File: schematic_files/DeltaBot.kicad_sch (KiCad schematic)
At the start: 16 parts, among them J1 USB C PD Modulle, J2 LIDAR, J3 MOTOR_L, J4 MOTOR_R, SW1 SW_SPDT, U1 Radxa_ROCK5B, U2 Buck Converter

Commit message: Updated PCB layout
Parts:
- removed D1, D2: D, deltabot:D_DO-41_SOD81_P10.16mm_Horizontal, symbol Device:D
- removed J2: LIDAR, deltabot:PinHeader_1x07_P2.54mm_Vertical, symbol Connector_Generic:Conn_01x07
- added J2: Conn_01x05, Connector_PinHeader_2.54mm:PinHeader_1x05_P2.54mm_Vertical, symbol Connector_Generic:Conn_01x05
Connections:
- net +5V: now also J2.2 (Pin_2)
- net GND: now also J2.5 (Pin_5)
- net LIDAR_RX: now also J2.4 (Pin_4)
- net LIDAR_TX: now also J2.3 (Pin_3)

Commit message: Small changes
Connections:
- net +5V: now also J2.1 (Pin_1); no longer J2.2 (Pin_2)
- net GND: now also J2.4 (Pin_4); no longer J2.5 (Pin_5)
- net LIDAR_RX: now also J2.3 (Pin_3); no longer J2.4 (Pin_4)
- net LIDAR_TX: now also J2.2 (Pin_2); no longer J2.3 (Pin_3)
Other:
- moved on the sheet: C3, J2
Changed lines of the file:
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@@
 	)
 	(junction
-		(at 34.29 119.38)
+		(at 24.13 104.14)
 		(diameter 0)
 		(color 0 0 0 0)
@@
 	)
 	(junction
-		(at 24.13 110.49)
+		(at 34.29 113.03)
 		(diameter 0)
 		(color 0 0 0 0)
@@
 	(wire
 		(pts
-			(xy 22.86 68.58) (xy 22.86 69.85)
+			(xy 34.29 113.03) (xy 34.29 114.3)
 		)
 		(stroke
@@
 	(wire
 		(pts
-			(xy 24.13 119.38) (xy 34.29 119.38)
+			(xy 22.86 68.58) (xy 22.86 69.85)
 		)
 		(stroke
@@
 	(wire
 		(pts
-			(xy 101.6 76.2) (xy 106.68 76.2)
+			(xy 24.13 113.03) (xy 34.29 113.03)
 		)
 		(stroke
@@
 	(wire
 		(pts
-			(xy 24.13 110.49) (xy 44.45 110.49)
+			(xy 101.6 76.2) (xy 106.68 76.2)
 		)
 		(stroke
@@
 	(wire
 		(pts
+			(xy 39.37 107.95) (xy 43.18 107.95)
+		)
+		(stroke
+			(width 0)
+			(type default)
+		)
+	)
+	(wire
+		(pts
 			(xy 66.04 64.77) (xy 76.2 64.77)
 		)
@@
 	(wire
 		(pts
-			(xy 34.29 119.38) (xy 40.64 119.38)
+			(xy 66.04 72.39) (xy 77.47 72.39)
 		)
 		(stroke
@@
 	(wire
 		(pts
-			(xy 66.04 72.39) (xy 77.47 72.39)
+			(xy 43.18 113.03) (xy 34.29 113.03)
 		)
 		(stroke
@@
 	(wire
 		(pts
-			(xy 68.58 97.79) (xy 68.58 102.87)
+			(xy 24.13 104.14) (xy 43.18 104.14)
 		)
 		(stroke
@@
 	(wire
 		(pts
-			(xy 104.14 83.82) (xy 106.68 83.82)
+			(xy 68.58 97.79) (xy 68.58 102.87)
 		)
 		(stroke
@@
 	(wire
 		(pts
-			(xy 66.04 102.87) (xy 68.58 102.87)
+			(xy 104.14 83.82) (xy 106.68 83.82)
 		)
 		(stroke
@@
 	(wire
 		(pts
-			(xy 40.64 119.38) (xy 40.64 118.11)
+			(xy 66.04 102.87) (xy 68.58 102.87)
 		)
 		(stroke
@@
 	(wire
 		(pts
-			(xy 24.13 111.76) (xy 24.13 110.49)
+			(xy 24.13 105.41) (xy 24.13 104.14)
 		)
 		(stroke
@@
 	(wire
 		(pts
-			(xy 34.29 120.65) (xy 34.29 119.38)
-		)
-		(stroke
-			(width 0)
-			(type default)
-		)
-	)
-	(wire
-		(pts
 			(xy 46.99 72.39) (xy 46.99 68.58)
 		)
@@
 	(wire
 		(pts
-			(xy 39.37 113.03) (xy 44.45 113.03)
-		)
-		(stroke
-			(width 0)
-			(type default)
-		)
-	)
-	(wire
-		(pts
 			(xy 22.86 64.77) (xy 25.4 64.77)
 		)
@@
 	(wire
 		(pts
+			(xy 39.37 110.49) (xy 43.18 110.49)
+		)
+		(stroke
+			(width 0)
+			(type default)
+		)
+	)
+	(wire
+		(pts
 			(xy 71.12 34.29) (xy 73.66 34.29)
 		)
@@
 	(wire
 		(pts
-			(xy 39.37 115.57) (xy 44.45 115.57)
-		)
-		(stroke
-			(width 0)
-			(type default)
-		)
-	)
-	(wire
-		(pts
 			(xy 168.91 26.67) (xy 176.53 26.67)
 		)
@@
 	(wire
 		(pts
-			(xy 40.64 118.11) (xy 44.45 118.11)
+			(xy 168.91 35.56) (xy 167.64 35.56)
 		)
 		(stroke
@@
 	(wire
 		(pts
-			(xy 168.91 35.56) (xy 167.64 35.56)
+			(xy 71.12 31.75) (xy 71.12 34.29)
 		)
 		(stroke
@@
 	(wire
 		(pts
-			(xy 71.12 31.75) (xy 71.12 34.29)
+			(xy 43.18 105.41) (xy 43.18 104.14)
 		)
 		(stroke
@@
 	(wire
 		(pts
-			(xy 21.59 110.49) (xy 24.13 110.49)
+			(xy 21.59 104.14) (xy 24.13 104.14)
 		)
 		(stroke
@@
 	(global_label "LIDAR_TX"
 		(shape input)
-		(at 39.37 113.03 180)
+		(at 39.37 107.95 180)
 		(effects
 			(font
@@
 		)
 		(property "Intersheetrefs" "${INTERSHEET_REFS}"
-			(at 39.37 113.03 0)
+			(at 39.37 107.95 0)
 			(effects
 				(font
@@
 	(global_label "LIDAR_RX"
 		(shape input)
-		(at 39.37 115.57 180)
+		(at 39.37 110.49 180)
 		(effects
 			(font
@@
 		)
 		(property "Intersheetrefs" "${INTERSHEET_REFS}"
-			(at 39.37 115.57 0)
+			(at 39.37 110.49 0)
 			(effects
 				(font
@@
 	(symbol
 		(lib_id "power:GND")
-		(at 34.29 120.65 0)
+		(at 34.29 114.3 0)
 		(unit 1)
 		(exclude_from_sim no)
@@
 		(dnp no)
 		(property "Reference" "#PWR09"
-			(at 34.29 127 0)
+			(at 34.29 120.65 0)
 			(effects
 				(font
@@
 		)
 		(property "Value" "GND"
-			(at 34.417 125.0442 0)
+			(at 34.417 118.6942 0)
 			(effects
 				(font
@@
 		)
 		(property "Footprint" ""
-			(at 34.29 120.65 0)
+			(at 34.29 114.3 0)
 			(effects
 				(font
@@
 		)
 		(property "Datasheet" ""
-			(at 34.29 120.65 0)
+			(at 34.29 114.3 0)
 			(effects
 				(font
@@
 		)
 		(property "Description" ""
-			(at 34.29 120.65 0)
+			(at 34.29 114.3 0)
 			(effects
 				(font
@@
 	(symbol
 		(lib_id "power:+5V")
-		(at 21.59 110.49 90)
+		(at 21.59 104.14 90)
 		(unit 1)
 		(exclude_from_sim no)
@@
 		(dnp no)
 		(property "Reference" "#PWR08"
-			(at 25.4 110.49 0)
+			(at 25.4 104.14 0)
 			(effects
 				(font
@@
 		)
 		(property "Value" "+5V"
-			(at 18.3388 110.109 90)
+			(at 18.3388 103.759 90)
 			(effects
 				(font
@@
 		)
 		(property "Footprint" ""
-			(at 21.59 110.49 0)
+			(at 21.59 104.14 0)
 			(effects
 				(font
@@
 		)
 		(property "Datasheet" ""
-			(at 21.59 110.49 0)
+			(at 21.59 104.14 0)
 			(effects
 				(font
@@
 		)
 		(property "Description" ""
-			(at 21.59 110.49 0)
+			(at 21.59 104.14 0)
 			(effects
 				(font
@@
 	(symbol
 		(lib_id "Connector_Generic:Conn_01x05")
-		(at 49.53 113.03 0)
+		(at 48.26 110.49 0)
 		(unit 1)
 		(exclude_from_sim no)
@@
 		(fields_autoplaced yes)
 		(property "Reference" "J2"
-			(at 52.07 111.7599 0)
+			(at 50.8 109.2199 0)
 			(effects
 				(font
@@
 		)
 		(property "Value" "Conn_01x05"
-			(at 52.07 114.2999 0)
+			(at 50.8 111.7599 0)
 			(effects
 				(font
@@
 		)
 		(property "Footprint" "Connector_PinHeader_2.54mm:PinHeader_1x05_P2.54mm_Vertical"
-			(at 49.53 113.03 0)
+			(at 48.26 110.49 0)
 			(effects
 				(font
@@
 		)
 		(property "Datasheet" "~"
-			(at 49.53 113.03 0)
+			(at 48.26 110.49 0)
 			(effects
 				(font
@@
 		)
 		(property "Description" "Generic connector, single row, 01x05, script generated (kicad-library-utils/schlib/autogen/connector/)"
-			(at 49.53 113.03 0)
+			(at 48.26 110.49 0)
 			(effects
 				(font
@@
 	(symbol
 		(lib_id "Device:C_Polarized")
-		(at 24.13 115.57 0)
+		(at 24.13 109.22 0)
 		(unit 1)
 		(exclude_from_sim no)
@@
 		(dnp no)
 		(property "Reference" "C3"
-			(at 17.526 114.554 0)
+			(at 17.526 108.204 0)
 			(effects
 				(font
@@
 		)
 		(property "Value" "1uF"
-			(at 17.526 117.094 0)
+			(at 17.526 110.744 0)
 			(effects
 				(font
@@
 		)
 		(property "Footprint" "deltabot:C_Disc_D3.0mm_W2.0mm_P2.50mm"
-			(at 25.0952 119.38 0)
+			(at 25.0952 113.03 0)
 			(effects
 				(font
@@
 		)
 		(property "Datasheet" "~"
-			(at 24.13 115.57 0)
+			(at 24.13 109.22 0)
 			(effects
 				(font
@@
 		)
 		(property "Description" "Polarized capacitor"
-			(at 24.13 115.57 0)
+			(at 24.13 109.22 0)
 			(effects
 				(font

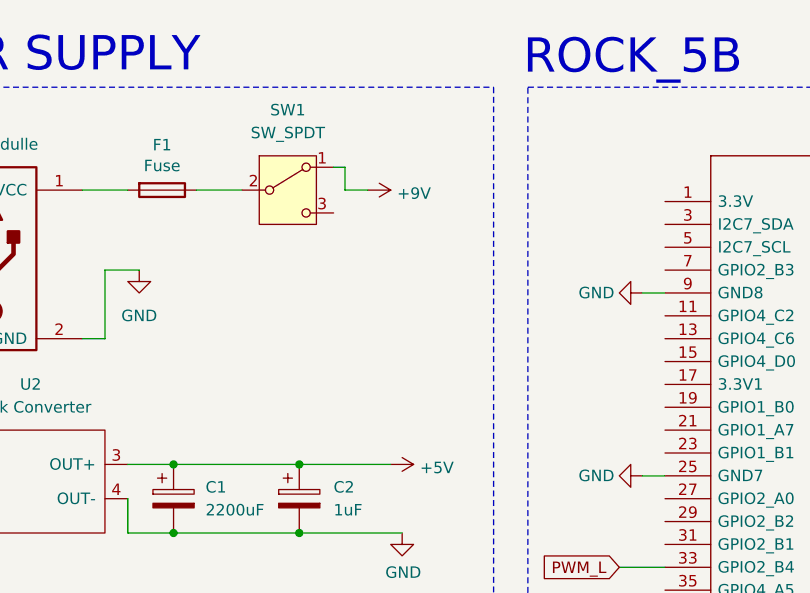
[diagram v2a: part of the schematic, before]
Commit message: Added an LED to it.
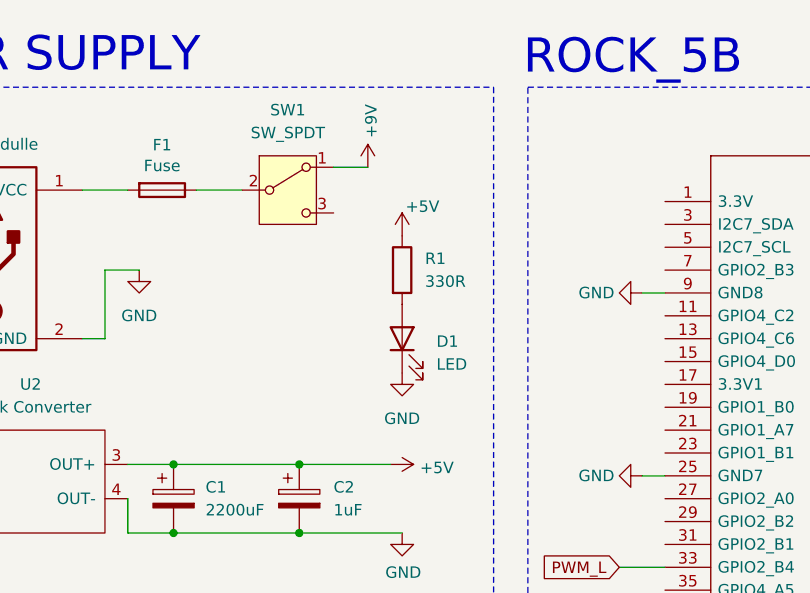
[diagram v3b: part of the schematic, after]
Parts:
- added D1: LED, LED_THT:LED_D5.0mm_Clear, symbol Device:LED
- added R1: 330R, Resistor_THT:R_Axial_DIN0207_L6.3mm_D2.5mm_P10.16mm_Horizontal, symbol Device:R
- J2: footprint Connector_PinHeader_2.54mm:PinHeader_1x05_P2.54mm_Vertical -> DeltaBotFootprints:PinHeader_1x05_P2.54mm_Vertical; symbol Connector_Generic:Conn_01x05 -> Deltabot:Conn_01x05
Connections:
- net +5V: now also R1.1
- net GND: now also D1.1 (K)
- new net: D1.2 (A), R1.2

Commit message: Fixed the USB PD module footprint.
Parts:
- J1: footprint deltabot:USB_C -> DeltaBotFootprints:USB_C; symbol deltabot.lib:USB C PD Connector -> Deltabot:USB C PD Connector
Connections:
- net GND: now also J1.4 (GND)
- net at F1.2, J1.1 (VCC): now also J1.3 (VCC)
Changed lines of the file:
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@@
 	)
 	(junction
+		(at 41.91 34.29)
+		(diameter 0)
+		(color 0 0 0 0)
+	)
+	(junction
+		(at 41.91 50.8)
+		(diameter 0)
+		(color 0 0 0 0)
+	)
+	(junction
 		(at 52.07 64.77)
 		(diameter 0)
@@
 	(wire
 		(pts
+			(xy 39.37 36.83) (xy 41.91 36.83)
+		)
+		(stroke
+			(width 0)
+			(type default)
+		)
+	)
+	(wire
+		(pts
 			(xy 63.5 119.38) (xy 69.85 119.38)
 		)
@@
 	(wire
 		(pts
-			(xy 104.14 66.04) (xy 106.68 66.04)
+			(xy 41.91 36.83) (xy 41.91 34.29)
 		)
 		(stroke
@@
 	(wire
 		(pts
-			(xy 44.45 43.18) (xy 48.26 43.18)
+			(xy 104.14 66.04) (xy 106.68 66.04)
 		)
 		(stroke
@@
 	(wire
 		(pts
+			(xy 39.37 48.26) (xy 41.91 48.26)
+		)
+		(stroke
+			(width 0)
+			(type default)
+		)
+	)
+	(wire
+		(pts
 			(xy 167.64 76.2) (xy 170.18 76.2)
 		)
@@
 	(wire
 		(pts
-			(xy 44.45 50.8) (xy 44.45 43.18)
+			(xy 104.14 45.72) (xy 106.68 45.72)
 		)
 		(stroke
@@
 	(wire
 		(pts
-			(xy 104.14 45.72) (xy 106.68 45.72)
+			(xy 68.58 92.71) (xy 69.85 92.71)
 		)
 		(stroke
@@
 	(wire
 		(pts
-			(xy 68.58 92.71) (xy 69.85 92.71)
+			(xy 63.5 95.25) (xy 69.85 95.25)
 		)
 		(stroke
@@
 	(wire
 		(pts
-			(xy 63.5 95.25) (xy 69.85 95.25)
+			(xy 41.91 48.26) (xy 41.91 50.8)
 		)
 		(stroke
@@
 	(wire
 		(pts
-			(xy 41.91 50.8) (xy 44.45 50.8)
+			(xy 41.91 50.8) (xy 48.26 50.8)
 		)
 		(stroke
@@
 	(symbol
 		(lib_id "power:GND")
-		(at 48.26 43.18 0)
+		(at 48.26 50.8 0)
 		(unit 1)
 		(body_style 1)
@@
 		(fields_autoplaced yes)
 		(property "Reference" "#PWR015"
-			(at 48.26 49.53 0)
+			(at 48.26 57.15 0)
 			(hide yes)
 			(show_name no)
@@
 		)
 		(property "Value" "GND"
-			(at 48.26 48.26 0)
+			(at 48.26 55.88 0)
 			(show_name no)
 			(do_not_autoplace no)
@@
 		)
 		(property "Footprint" ""
-			(at 48.26 43.18 0)
+			(at 48.26 50.8 0)
 			(hide yes)
 			(show_name no)
@@
 		)
 		(property "Datasheet" ""
-			(at 48.26 43.18 0)
+			(at 48.26 50.8 0)
 			(hide yes)
 			(show_name no)
@@
 		)
 		(property "Description" "Power symbol creates a global label with name \"GND\" , ground"
-			(at 48.26 43.18 0)
+			(at 48.26 50.8 0)
 			(hide yes)
 			(show_name no)
@@
 	)
 	(symbol
-		(lib_id "deltabot.lib:USB C PD Connector")
+		(lib_id "Deltabot:USB C PD Connector")
 		(at 31.75 44.45 0)
 		(unit 1)
@@
 			)
 		)
-		(property "Footprint" "deltabot:USB_C"
+		(property "Footprint" "DeltaBotFootprints:USB_C"
 			(at 35.56 41.91 0)
 			(hide yes)
@@
 		(pin "2"
 		)
+		(pin "4"
+		)
+		(pin "3"
+		)
 		(instances
